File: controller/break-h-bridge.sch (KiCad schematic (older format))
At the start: 21 parts, among them J24 CONN_01X02, U7 74LS04, U8 VNH3SP30

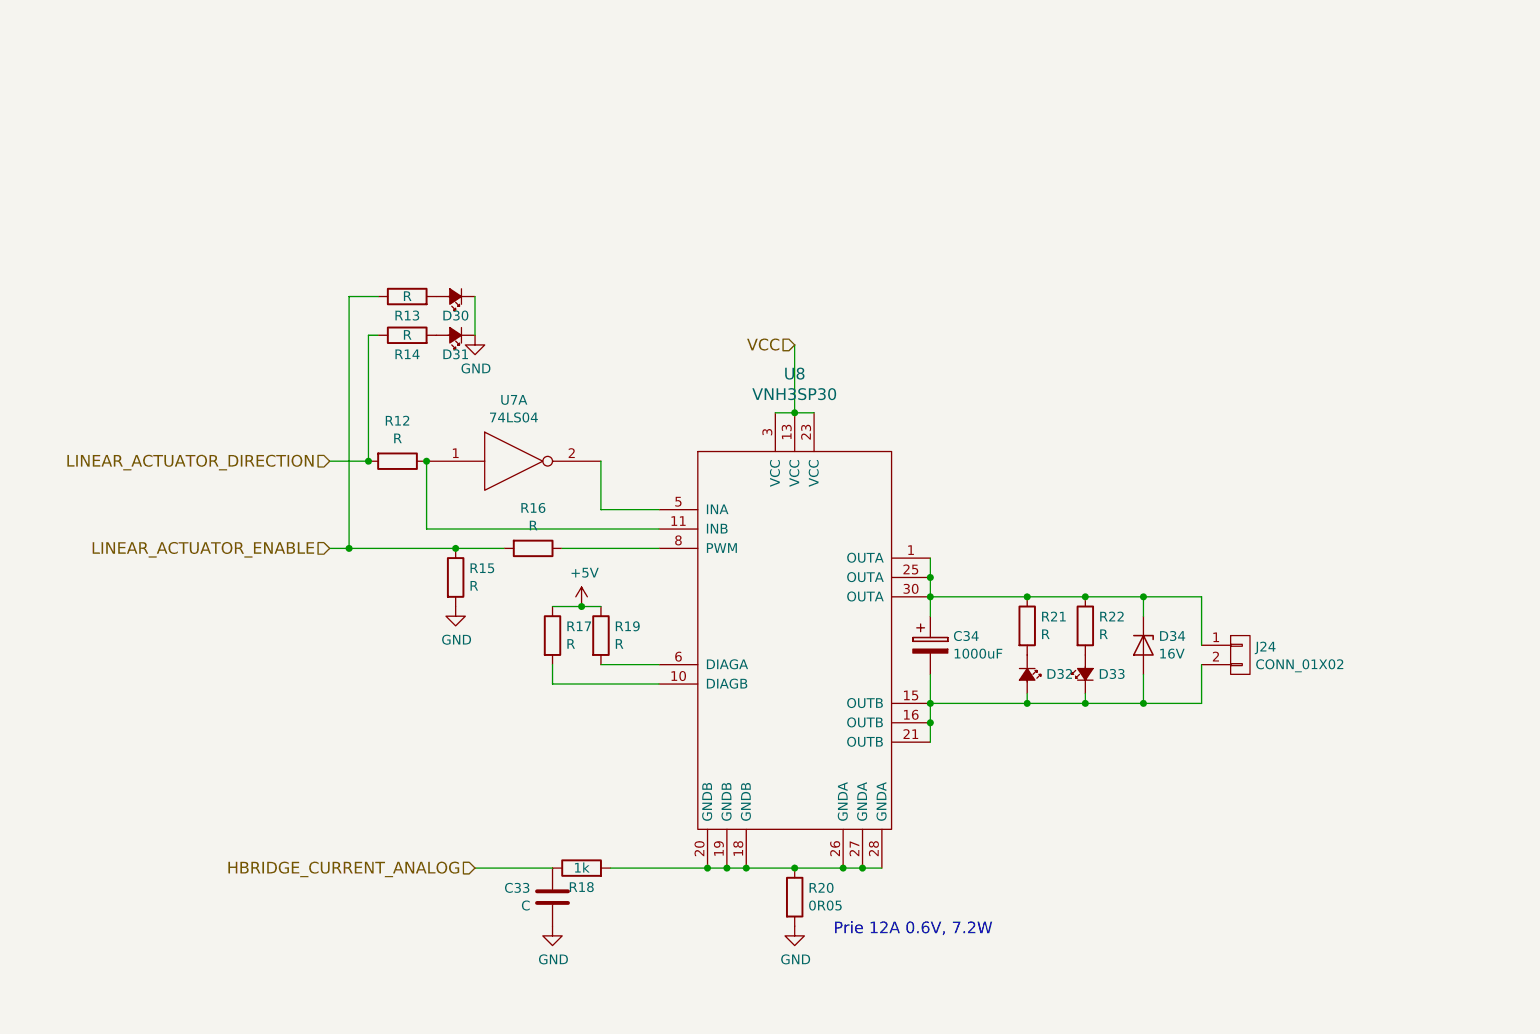
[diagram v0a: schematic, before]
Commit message: Change gas pedal interface so that it supports going up and down from the middle voltage so that it's compatible with Linde forklift gas mechanism
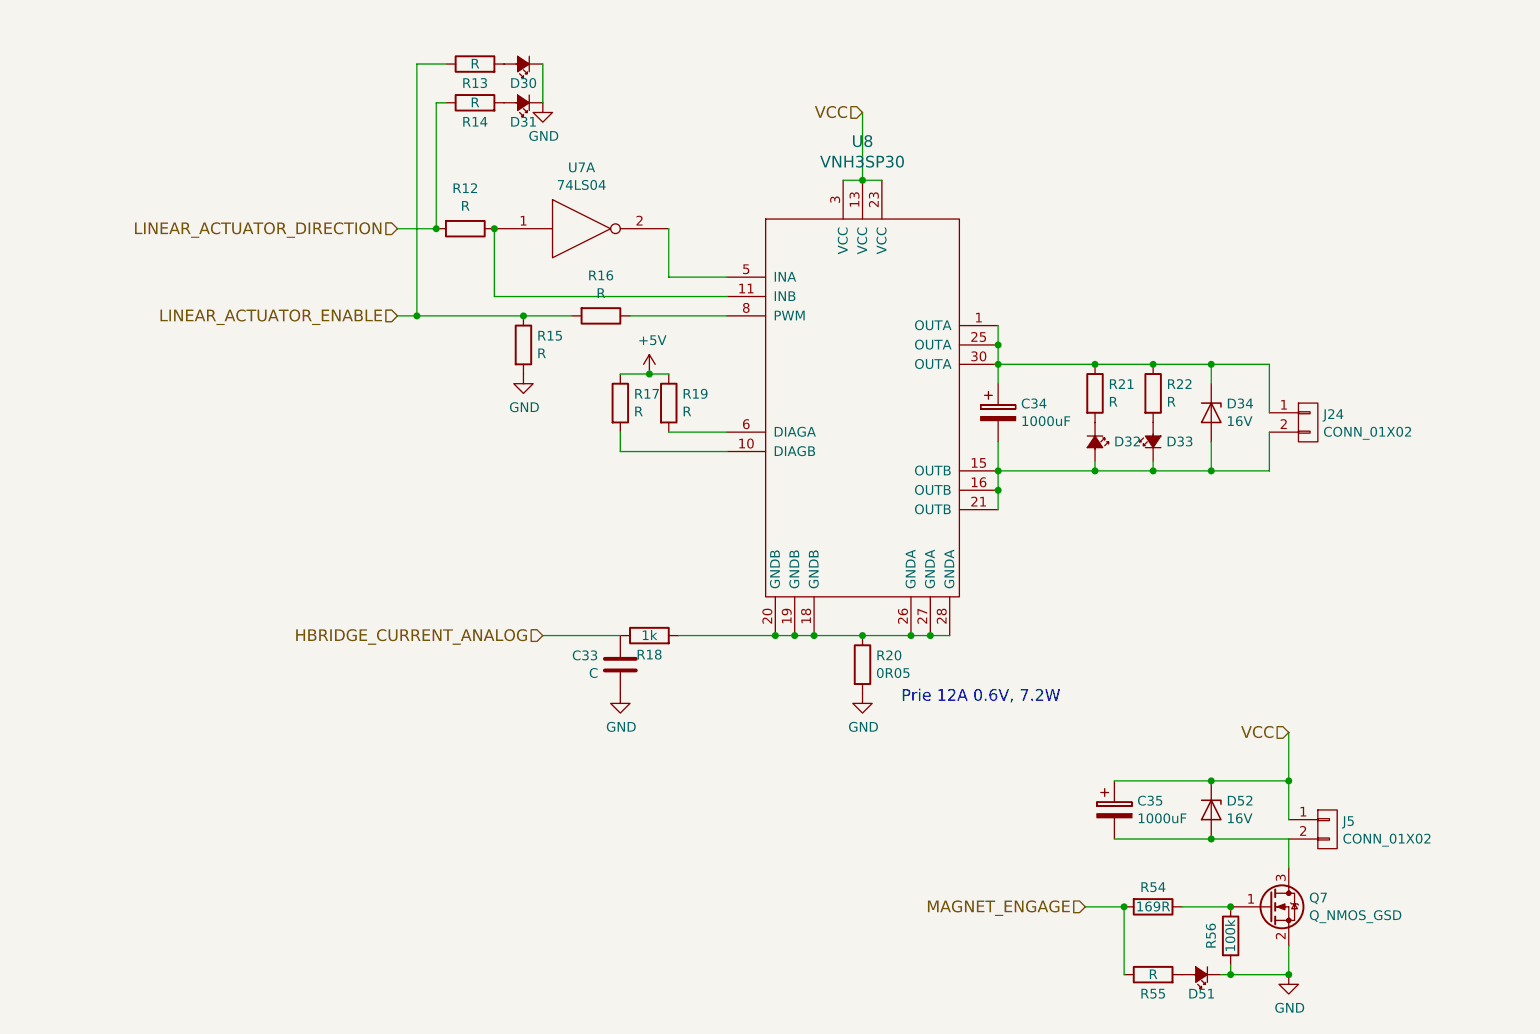
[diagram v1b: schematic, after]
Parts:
- added C35: 1000uF, symbol CP
- added D51: LED_Small_ALT, LEDs:LED_0805, symbol LED_Small_ALT
- added D52: 16V, symbol D_Zener
- added J5: CONN_01X02, symbol CONN_01X02
- added Q7: Q_NMOS_GSD, symbol Q_NMOS_GSD
- added R54: 169R, Resistors_SMD:R_0603_HandSoldering, symbol R
- added R55: R, Resistors_SMD:R_0603_HandSoldering, symbol R
- added R56: 100k, Resistors_SMD:R_0603_HandSoldering, symbol R
- C33: footprint (none) -> Capacitors_SMD:C_0603_HandSoldering
- D30, D31, D32, D33: footprint (none) -> LEDs:LED_0805
- R12, R13, R14, R15, R16, R17, R18, R19, R21, R22: footprint (none) -> Resistors_SMD:R_0603_HandSoldering
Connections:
- net GND: now also D51.1 (K), Q7.2 (S), R56.2
- net VCC: now also C35.1, D52.1 (K), J5.1 (P1)
- new net: C35.2, D52.2 (A), J5.2 (P2), Q7.3 (D)
- new net: Q7.1 (G), R54.1, R56.1
- new net: D51.2 (A), R55.2
- new net MAGNET_ENGAGE: R54.2, R55.1
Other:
- moved on the sheet: C33, C34, D30, D31, D32, D33, D34, J24, R12, R13, R14, R15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

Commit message: More or less final controller board
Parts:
- removed C34, C35: 1000uF, symbol CP
- removed D34, D52: 16V, symbol D_Zener
- added C40, C41, C42: 470u, Capacitors_ThroughHole:CP_Radial_D16.0mm_P7.50mm, symbol CP1
- added D56, D57: 16V, Diodes_SMD:D_SMB_Handsoldering, symbol D_Zener
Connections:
- net VCC: now also C42.1, D56.1 (K)
- net at J5.2 (P2), Q7.3 (D): now also C42.2, D56.2 (A)
- net at J24.1 (P1), R21.1, R22.1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: now also C40.1, C41.1, D57.1 (K)
- net at D32.2 (A), D33.1 (K), J24.2 (P2)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: now also C40.2, C41.2, D57.2 (A)
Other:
- moved on the sheet: D32, D33, J24, R21, R22
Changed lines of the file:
@@
 LIBS:valves
 LIBS:mic-parts
+LIBS:shield_arduino
 LIBS:controller-cache
 EELAYER 26 0
@@
 L CONN_01X02 J24
 U 1 1 58D1C1D0
-P 8550 2700
-F 0 "J24" H 8628 2741 50  0000 L CNN
-F 1 "CONN_01X02" H 8628 2650 50  0000 L CNN
-F 2 "" H -650 -1250 50  0001 C CNN
-F 3 "" H -650 -1250 50  0001 C CNN
-	1    8550 2700
+P 9050 2700
+F 0 "J24" H 9128 2741 50  0000 L CNN
+F 1 "CONN_01X02" H 9128 2650 50  0000 L CNN
+F 2 "" H -150 -1250 50  0001 C CNN
+F 3 "" H -150 -1250 50  0001 C CNN
+	1    9050 2700
 	1    0    0    -1
 $EndComp
@@
 	5000 2450 5250 2450
 $Comp
-L +5V #PWR11
+L +5V #PWR016
 U 1 1 58D1C43C
 P 5150 2450
-F 0 "#PWR11" H 5200 2500 50  0001 C CNN
+F 0 "#PWR016" H 5200 2500 50  0001 C CNN
 F 1 "+5V" H 5165 2623 50  0000 C CNN
 F 2 "" H -2600 -700 50  0001 C CNN
@@
 Connection ~ 4500 2150
 $Comp
-L GND #PWR12
+L GND #PWR017
 U 1 1 58D1C737
 P 6250 4100
-F 0 "#PWR12" H 6300 4150 50  0001 C CNN
+F 0 "#PWR017" H 6300 4150 50  0001 C CNN
 F 1 "GND" H 6255 3927 50  0000 C CNN
 F 2 "" H -1000 1050 50  0001 C CNN
@@
 $EndComp
 $Comp
-L GND #PWR8
+L GND #PWR018
 U 1 1 58D1C755
 P 4500 2450
-F 0 "#PWR8" H 4550 2500 50  0001 C CNN
+F 0 "#PWR018" H 4550 2500 50  0001 C CNN
 F 1 "GND" H 4505 2277 50  0000 C CNN
 F 2 "" H -2750 -600 50  0001 C CNN
@@
 Text HLabel 3850 1700 0    60   Input ~ 0
 LINEAR_ACTUATOR_DIRECTION
-$Comp
-L CP C34
-U 1 1 58D1CF44
-P 6950 2650
-F 0 "C34" H 7068 2696 50  0000 L CNN
-F 1 "1000uF" H 7068 2605 50  0000 L CNN
-F 2 "" H -62 -1400 50  0001 C CNN
-F 3 "" H -100 -1250 50  0001 C CNN
-	1    6950 2650
-	1    0    0    -1
-$EndComp
-Wire Wire Line
-	6950 2400 8350 2400
-Wire Wire Line
-	8350 2400 8350 2650
-Wire Wire Line
-	6950 2950 8350 2950
-Wire Wire Line
-	8350 2950 8350 2750
-$Comp
-L D_Zener D34
-U 1 1 58D1D143
-P 8050 2650
-F 0 "D34" V 8004 2729 50  0000 L CNN
-F 1 "16V" V 8095 2729 50  0000 L CNN
-F 2 "" H 850 -1150 50  0001 C CNN
-F 3 "" H 850 -1150 50  0001 C CNN
-	1    8050 2650
-	0    1    1    0
-$EndComp
-Wire Wire Line
-	8050 2500 8050 2400
-Connection ~ 8050 2400
-Wire Wire Line
-	8050 2800 8050 2950
-Connection ~ 8050 2950
+Wire Wire Line
+	6950 2400 8850 2400
+Wire Wire Line
+	8850 2400 8850 2650
+Wire Wire Line
+	6950 2950 8850 2950
+Wire Wire Line
+	8850 2950 8850 2750
+Wire Wire Line
+	8550 2500 8550 2400
+Connection ~ 8550 2400
+Wire Wire Line
+	8550 2800 8550 2950
+Connection ~ 8550 2950
 $Comp
 L R R12
@@
 L R R21
 U 1 1 58D3D1D4
-P 7450 2550
-F 0 "R21" H 7520 2596 50  0000 L CNN
-F 1 "R" H 7520 2505 50  0000 L CNN
-F 2 "Resistors_SMD:R_0603_HandSoldering" V 2480 -1150 50  0001 C CNN
-F 3 "" H 2550 -1150 50  0001 C CNN
-	1    7450 2550
+P 7950 2550
+F 0 "R21" H 8020 2596 50  0000 L CNN
+F 1 "R" H 8020 2505 50  0000 L CNN
+F 2 "Resistors_SMD:R_0603_HandSoldering" V 2980 -1150 50  0001 C CNN
+F 3 "" H 3050 -1150 50  0001 C CNN
+	1    7950 2550
 	1    0    0    -1
 $EndComp
@@
 L R R22
 U 1 1 58D3D22C
-P 7750 2550
-F 0 "R22" H 7820 2596 50  0000 L CNN
-F 1 "R" H 7820 2505 50  0000 L CNN
-F 2 "Resistors_SMD:R_0603_HandSoldering" V 2780 -1150 50  0001 C CNN
-F 3 "" H 2850 -1150 50  0001 C CNN
-	1    7750 2550
+P 8250 2550
+F 0 "R22" H 8320 2596 50  0000 L CNN
+F 1 "R" H 8320 2505 50  0000 L CNN
+F 2 "Resistors_SMD:R_0603_HandSoldering" V 3280 -1150 50  0001 C CNN
+F 3 "" H 3350 -1150 50  0001 C CNN
+	1    8250 2550
 	1    0    0    -1
 $EndComp
@@
 L LED_Small_ALT D32
 U 1 1 58D3D2B4
-P 7450 2800
-F 0 "D32" V 7450 2898 50  0000 L CNN
-F 1 "LED_Small_ALT" V 7495 2898 50  0001 L CNN
-F 2 "LEDs:LED_0805" V -2950 -1400 50  0001 C CNN
-F 3 "" V -2950 -1400 50  0001 C CNN
-	1    7450 2800
+P 7950 2800
+F 0 "D32" V 7950 2898 50  0000 L CNN
+F 1 "LED_Small_ALT" V 7995 2898 50  0001 L CNN
+F 2 "LEDs:LED_0805" V -2450 -1400 50  0001 C CNN
+F 3 "" V -2450 -1400 50  0001 C CNN
+	1    7950 2800
 	0    1    1    0
 $EndComp
@@
 L LED_Small_ALT D33
 U 1 1 58D3D34F
-P 7750 2800
-F 0 "D33" V 7750 2732 50  0000 R CNN
-F 1 "LED_Small_ALT" V 7705 2732 50  0001 R CNN
-F 2 "LEDs:LED_0805" V -2650 -1400 50  0001 C CNN
-F 3 "" V -2650 -1400 50  0001 C CNN
-	1    7750 2800
+P 8250 2800
+F 0 "D33" V 8250 2732 50  0000 R CNN
+F 1 "LED_Small_ALT" V 8205 2732 50  0001 R CNN
+F 2 "LEDs:LED_0805" V -2150 -1400 50  0001 C CNN
+F 3 "" V -2150 -1400 50  0001 C CNN
+	1    8250 2800
 	0    -1   -1   0
 $EndComp
 Wire Wire Line
-	7750 2900 7750 2950
-Connection ~ 7750 2950
-Wire Wire Line
-	7450 2900 7450 2950
-Connection ~ 7450 2950
-Connection ~ 7450 2400
-Connection ~ 7750 2400
+	8250 2900 8250 2950
+Connection ~ 8250 2950
+Wire Wire Line
+	7950 2900 7950 2950
+Connection ~ 7950 2950
+Connection ~ 7950 2400
+Connection ~ 8250 2400
 Connection ~ 5800 3800
 Text HLabel 4600 3800 0    60   Input ~ 0
@@
 $EndComp
 $Comp
-L GND #PWR9
+L GND #PWR019
 U 1 1 58D46703
 P 4600 1050
-F 0 "#PWR9" H 4650 1100 50  0001 C CNN
+F 0 "#PWR019" H 4650 1100 50  0001 C CNN
 F 1 "GND" H 4605 877 50  0000 C CNN
 F 2 "" H -2650 -2000 50  0001 C CNN
@@
 $EndComp
 $Comp
-L GND #PWR10
+L GND #PWR020
 U 1 1 58D46D16
 P 5000 4100
-F 0 "#PWR10" H 5050 4150 50  0001 C CNN
+F 0 "#PWR020" H 5050 4150 50  0001 C CNN
 F 1 "GND" H 5005 3927 50  0000 C CNN
 F 2 "" H -2250 1050 50  0001 C CNN
@@
 	8450 4300 8450 4750
 $Comp
-L GND #PWR13
+L GND #PWR021
 U 1 1 58C85705
 P 8450 5550
-F 0 "#PWR13" H 8500 5600 50  0001 C CNN
+F 0 "#PWR021" H 8500 5600 50  0001 C CNN
 F 1 "GND" H 8455 5377 50  0000 C CNN
 F 2 "" H 1200 2500 50  0001 C CNN
@@
 MAGNET_ENGAGE
 $Comp
-L D_Zener D52
-U 1 1 58C86524
-P 8050 4700
-F 0 "D52" V 8004 4779 50  0000 L CNN
-F 1 "16V" V 8095 4779 50  0000 L CNN
-F 2 "" H 850 900 50  0001 C CNN
-F 3 "" H 850 900 50  0001 C CNN
-	1    8050 4700
-	0    1    1    0
-$EndComp
-$Comp
 L LED_Small_ALT D51
 U 1 1 58C86A0A
@@
 Wire Wire Line
 	7550 4850 8450 4850
-$Comp
-L CP C35
-U 1 1 58C87110
-P 7550 4700
-F 0 "C35" H 7668 4746 50  0000 L CNN
-F 1 "1000uF" H 7668 4655 50  0000 L CNN
-F 2 "" H 538 650 50  0001 C CNN
-F 3 "" H 500 800 50  0001 C CNN
-	1    7550 4700
-	1    0    0    -1
-$EndComp
 Connection ~ 8050 4550
 Connection ~ 8050 4850
+$Comp
+L D_Zener D57
+U 1 1 58C9AE19
+P 8550 2650
+F 0 "D57" V 8504 2729 50  0000 L CNN
+F 1 "16V" V 8595 2729 50  0000 L CNN
+F 2 "Diodes_SMD:D_SMB_Handsoldering" H 3250 1050 50  0001 C CNN
+F 3 "" H 3250 1050 50  0001 C CNN
+F 4 "1SMB5930BT3G" H 8550 2650 60  0001 C CNN "PartNo"
+F 5 "ON SEMI" H 8550 2650 60  0001 C CNN "Manufacturer"
+F 6 "1431172" H 8550 2650 60  0001 C CNN "Distributor"
+	1    8550 2650
+	0    1    1    0
+$EndComp
+$Comp
+L D_Zener D56
+U 1 1 58C9B041
+P 8050 4700
+F 0 "D56" V 8004 4779 50  0000 L CNN
+F 1 "16V" V 8095 4779 50  0000 L CNN
+F 2 "Diodes_SMD:D_SMB_Handsoldering" H 2750 3100 50  0001 C CNN
+F 3 "" H 2750 3100 50  0001 C CNN
+F 4 "1SMB5930BT3G" H 8050 4700 60  0001 C CNN "PartNo"
+F 5 "ON SEMI" H 8050 4700 60  0001 C CNN "Manufacturer"
+F 6 "1431172" H 8050 4700 60  0001 C CNN "Distributor"
+	1    8050 4700
+	0    1    1    0
+$EndComp
+$Comp
+L CP1 C42
+U 1 1 58CA022B
+P 7550 4700
+F 0 "C42" H 7665 4746 50  0000 L CNN
+F 1 "470u" H 7665 4655 50  0000 L CNN
+F 2 "Capacitors_ThroughHole:CP_Radial_D16.0mm_P7.50mm" H 2400 2950 50  0001 C CNN
+F 3 "" H 2400 2950 50  0001 C CNN
+F 4 "ECA2AAM471X" H 7550 4700 60  0001 C CNN "PartNo"
+F 5 "PANASONIC" H 7550 4700 60  0001 C CNN "Manufacturer"
+F 6 "8767696" H 7550 4700 60  0001 C CNN "Distributor"
+	1    7550 4700
+	-1   0    0    -1
+$EndComp
+$Comp
+L CP1 C40
+U 1 1 58CA0450
+P 6950 2650
+F 0 "C40" H 7065 2696 50  0000 L CNN
+F 1 "470u" H 7065 2605 50  0000 L CNN
+F 2 "Capacitors_ThroughHole:CP_Radial_D16.0mm_P7.50mm" H 1800 900 50  0001 C CNN
+F 3 "" H 1800 900 50  0001 C CNN
+F 4 "ECA2AAM471X" H 6950 2650 60  0001 C CNN "PartNo"
+F 5 "PANASONIC" H 6950 2650 60  0001 C CNN "Manufacturer"
+F 6 "8767696" H 6950 2650 60  0001 C CNN "Distributor"
+	1    6950 2650
+	1    0    0    -1
+$EndComp
+$Comp
+L CP1 C41
+U 1 1 58CA0587
+P 7400 2650
+F 0 "C41" H 7515 2696 50  0000 L CNN
+F 1 "470u" H 7515 2605 50  0000 L CNN
+F 2 "Capacitors_ThroughHole:CP_Radial_D16.0mm_P7.50mm" H 2250 900 50  0001 C CNN
+F 3 "" H 2250 900 50  0001 C CNN
+F 4 "ECA2AAM471X" H 7400 2650 60  0001 C CNN "PartNo"
+F 5 "PANASONIC" H 7400 2650 60  0001 C CNN "Manufacturer"
+F 6 "8767696" H 7400 2650 60  0001 C CNN "Distributor"
+	1    7400 2650
+	1    0    0    -1
+$EndComp
+Wire Wire Line
+	7400 2500 7400 2400
+Connection ~ 7400 2400
+Wire Wire Line
+	7400 2800 7400 2950
+Connection ~ 7400 2950
 $EndSCHEMATC

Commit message: Some progress with controller board routing
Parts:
- Q7: footprint (none) -> TO_SOT_Packages_SMD:TO-252-2Lead; Distributor (none) -> 2317615; Manufacturer (none) -> ?; PartNo (none) -> ?
- U8: footprint (none) -> smalsiukas-footpints:SOIC-30
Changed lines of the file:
@@
 F 0 "U8" H 6250 3450 60  0000 C CNN
 F 1 "VNH3SP30" H 6250 3344 60  0000 C CNN
-F 2 "" H 250 -900 60  0001 C CNN
+F 2 "smalsiukas-footpints:SOIC-30" H 250 -900 60  0001 C CNN
 F 3 "" H 250 -900 60  0001 C CNN
 F 4 "?" H 6250 2350 60  0001 C CNN "PartNo"
@@
 	5000 2450 5250 2450
 $Comp
-L +5V #PWR016
+L +5V #PWR018
 U 1 1 58D1C43C
 P 5150 2450
-F 0 "#PWR016" H 5200 2500 50  0001 C CNN
+F 0 "#PWR018" H 5200 2500 50  0001 C CNN
 F 1 "+5V" H 5165 2623 50  0000 C CNN
 F 2 "" H -2600 -700 50  0001 C CNN
@@
 Connection ~ 4500 2150
 $Comp
-L GND #PWR017
+L GND #PWR019
 U 1 1 58D1C737
 P 6250 4100
-F 0 "#PWR017" H 6300 4150 50  0001 C CNN
+F 0 "#PWR019" H 6300 4150 50  0001 C CNN
 F 1 "GND" H 6255 3927 50  0000 C CNN
 F 2 "" H -1000 1050 50  0001 C CNN
@@
 $EndComp
 $Comp
-L GND #PWR018
+L GND #PWR020
 U 1 1 58D1C755
 P 4500 2450
-F 0 "#PWR018" H 4550 2500 50  0001 C CNN
+F 0 "#PWR020" H 4550 2500 50  0001 C CNN
 F 1 "GND" H 4505 2277 50  0000 C CNN
 F 2 "" H -2750 -600 50  0001 C CNN
@@
 $EndComp
 $Comp
-L GND #PWR019
+L GND #PWR021
 U 1 1 58D46703
 P 4600 1050
-F 0 "#PWR019" H 4650 1100 50  0001 C CNN
+F 0 "#PWR021" H 4650 1100 50  0001 C CNN
 F 1 "GND" H 4605 877 50  0000 C CNN
 F 2 "" H -2650 -2000 50  0001 C CNN
@@
 $EndComp
 $Comp
-L GND #PWR020
+L GND #PWR022
 U 1 1 58D46D16
 P 5000 4100
-F 0 "#PWR020" H 5050 4150 50  0001 C CNN
+F 0 "#PWR022" H 5050 4150 50  0001 C CNN
 F 1 "GND" H 5005 3927 50  0000 C CNN
 F 2 "" H -2250 1050 50  0001 C CNN
@@
 	8450 4300 8450 4750
 $Comp
-L GND #PWR021
+L GND #PWR023
 U 1 1 58C85705
 P 8450 5550
-F 0 "#PWR021" H 8500 5600 50  0001 C CNN
+F 0 "#PWR023" H 8500 5600 50  0001 C CNN
 F 1 "GND" H 8455 5377 50  0000 C CNN
 F 2 "" H 1200 2500 50  0001 C CNN
@@
 F 0 "Q7" H 8555 5246 50  0000 L CNN
 F 1 "Q_NMOS_GSD" H 8555 5155 50  0000 L CNN
-F 2 "" H 8550 5300 50  0001 C CNN
+F 2 "TO_SOT_Packages_SMD:TO-252-2Lead" H 8550 5300 50  0001 C CNN
 F 3 "" H 8350 5200 50  0001 C CNN
+F 4 "?" H 8350 5200 60  0001 C CNN "PartNo"
+F 5 "?" H 8350 5200 60  0001 C CNN "Manufacturer"
+F 6 "2317615" H 8350 5200 60  0001 C CNN "Distributor"
 	1    8350 5200
 	1    0    0    -1

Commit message: Finish the routing, add some significant fixes: *correct to-252 pin numbering * longer pads for relays * fix footprint of the optocouplers
Also finish the routing
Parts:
- added C46: C, Capacitors_SMD:C_0603_HandSoldering, symbol C
- added C47: 1u, Capacitors_SMD:C_1210_HandSoldering, symbol C
- added D36: 5V, Diodes_SMD:SOD-123, symbol D_Zener
- D30, D31, D32, D33, D51: footprint LEDs:LED_0805 -> LEDs:LED_D5.0mm; Distributor (none) -> ?; Manufacturer (none) -> ?; PartNo (none) -> ?
- J24, J5: footprint (none) -> Connectors_Terminal_Blocks:TerminalBlock_Pheonix_MKDS1.5-2pol; Distributor (none) -> ?; Manufacturer (none) -> ?; PartNo (none) -> ?
- Q7: symbol Q_NMOS_GSD -> Q_NMOS_GDS
- R20: footprint (none) -> TO_SOT_Packages_THT:TO-220-2_Vertical; Distributor (none) -> 2328295; Manufacturer (none) -> ?; PartNo (none) -> ?
- U7: value 74LS04 -> SN74AHCT1G14DBVR; symbol 74LS04 -> SN74AHCT1G14DBVR; Distributor ? -> 1105925; Manufacturer ? -> TEXAS INSTRUMENTS; PartNo 1236329 -> SN74AHCT1G14DBVR
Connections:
- wire segments 42 -> 46
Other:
- moved on the sheet: C33, D30, D31, R12, R13, R14
